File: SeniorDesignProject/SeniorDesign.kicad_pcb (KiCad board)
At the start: 2 copper layers, 31 parts, among them J1 RJ45(LoadCells), J2 RJ45(Accelerometer), J3 PICkit3, J4 RJ11(ICD3), J5 ID-12LA Header, J6 XBEE Header, J7 7-Segment Display, P7 Power 1, P9 Power 2, U1 INA827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

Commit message: added some traces
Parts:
- C1: footprint Capacitors_SMD:C_0201 -> Capacitors_SMD:C_0805
- R1: moved to B.Cu
- moved P7 118.7 mm to (20.0, 59.5)
- moved JP1 116.6 mm to (44.5, 52.0)
- moved U10 114.3 mm to (37.0, 83.5)
- moved C6 112.4 mm to (116.5, 69.1), turned to 90 degrees
- moved C7 108.4 mm to (107.2, 58.5)
- moved R2 102.1 mm to (98.6, 66.1)
- moved JP2 101.3 mm to (42.8, 40.5)
- moved P9 99.2 mm to (21.4, 83.1)
- moved J6 93.4 mm to (82.1, 24.8)
- moved R4 90.5 mm to (121.2, 68.5), turned to 180 degrees
- moved C2 88.3 mm to (101.3, 82.7), turned to 90 degrees
- moved C8 84.8 mm to (113.5, 56.9), turned to 270 degrees
- moved U9 83.6 mm to (51.5, 83.1)
- moved R3 81.7 mm to (121.2, 65.1)
- moved G*** 79.6 mm to (65.6, 128.9)
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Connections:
- CPU1 pad 13: AN0 -> Net-(CPU1-Pad13)
- CPU1 pad 28: Net-(CPU1-Pad28) -> AN0
- CPU1 pad 31: SDA2 -> Net-(CPU1-Pad31)
- CPU1 pad 32: SCL2 -> Net-(CPU1-Pad32)
- CPU1 pad 36: SDA1 -> Net-(CPU1-Pad36)
- CPU1 pad 37: SCL1 -> Net-(CPU1-Pad37)
- CPU1 pad 43: Net-(CPU1-Pad43) -> SDA2
- CPU1 pad 44: Net-(CPU1-Pad44) -> SCL2
- CPU1 pad 45: Net-(CPU1-Pad45) -> UART1RX
- CPU1 pad 46: Net-(CPU1-Pad46) -> UART1TX
- CPU1 pad 48: Net-(CPU1-Pad48) -> SCL1
- CPU1 pad 49: Net-(CPU1-Pad49) -> SDA1
- CPU1 pad 50: UART1TX -> Net-(CPU1-Pad50)
- CPU1 pad 51: UART1RX -> Net-(CPU1-Pad51)
- U1 pad 1: Net-(R1-Pad1) -> A-
- U1 pad 2: A- -> Net-(R1-Pad1)
- U1 pad 3: A+ -> Net-(R1-Pad2)
- U1 pad 4: -5V -> A+
- U1 pad 5: Net-(U1-Pad5) -> -5V
- U1 pad 6: AN0 -> Net-(U1-Pad6)
- U1 pad 7: Net-(U1-Pad7) -> AN0
- U1 pad 8: Net-(R1-Pad2) -> +5V
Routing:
- net GND: track 0.00 -> 91.7 mm
- net UART2RX: track 0.00 -> 59.2 mm, vias 0 -> 2
- net UART2TX: track 0.00 -> 57.5 mm
- net PGEC3: track 0.00 -> 33.3 mm
- net PGED3: track 0.00 -> 32.8 mm, vias 0 -> 2
- net 3.3V: track 0.00 -> 25.8 mm
- net UART1RX: track 0.00 -> 20.5 mm, vias 0 -> 2
- net A+: track 0.00 -> 12.9 mm
- net A-: track 0.00 -> 10.6 mm
- net SCL1: track 0.00 -> 8.48 mm
- net SCL2: track 0.00 -> 7.47 mm
- net +5V: track 0.00 -> 5.66 mm
- net Net-(R1-Pad2): track 0.00 -> 5.29 mm, vias 0 -> 1
- net Net-(R1-Pad1): track 0.00 -> 4.77 mm, vias 0 -> 1
- net Net-(CPU1-Pad7): track 0.00 -> 3.64 mm
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
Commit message: Updates to board
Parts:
- moved G*** 133.3 mm to (197.9, 112.9)
- moved G*** 91.4 mm to (105.5, 41.7)
- moved C6 68.7 mm to (181.9, 90.4), turned to 0 degrees
- moved J5 67.6 mm to (198.2, 81.7)
- moved C2 67.6 mm to (165.8, 103.0)
- moved C7 67.6 mm to (171.7, 78.9)
- moved R5 67.6 mm to (183.9, 78.9)
- moved U9 67.6 mm to (116.0, 103.4)
- moved C1 67.6 mm to (176.7, 102.7)
- moved C8 67.6 mm to (178.0, 77.2)
- moved CPU1 67.6 mm to (172.4, 89.1)
- moved J1 67.6 mm to (167.5, 119.2)
- moved J3 67.6 mm to (136.4, 95.8)
- moved J4 67.6 mm to (87.0, 56.0)
- moved J6 67.6 mm to (146.6, 45.2)
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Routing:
- net GND: track 91.7 -> 35.6 mm
- net 3.3V: track 25.8 -> 21.0 mm
- net Net-(CPU1-Pad7): track 3.64 -> 4.75 mm

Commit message: Updates to board
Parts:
- removed JP1, JP2: Jumper_NO_Small, Pin_Headers:Pin_Header_Straight_1x02_Pitch2.54mm
- added U2: LM1117-3.3, TO_SOT_Packages_SMD:SOT-223, F.Cu at (82.6, 100.6)
- C5, C6, C7: moved to B.Cu
- J5: footprint Pin_Headers:Pin_Header_Straight_2x06_Pitch2.54mm -> Socket_Strips:Socket_Strip_Straight_1x05_Pitch2.54mm
- moved U9 31.0 mm to (97.3, 78.7)
- moved P9 26.6 mm to (81.6, 77.1), turned to 90 degrees
- moved J4 16.2 mm to (87.1, 39.8)
- moved R6 15.4 mm to (180.9, 89.6), turned to 270 degrees
- moved U10 15.0 mm to (110.6, 91.9)
- moved R3 12.1 mm to (182.3, 97.1)
- moved R5 11.8 mm to (183.1, 90.7), turned to 270 degrees
- moved R4 11.4 mm to (182.4, 99.7)
- moved G*** 11.3 mm to (116.5, 44.0)
- moved P7 7.88 mm to (81.6, 87.2), turned to 90 degrees
- moved C7 7.33 mm to (173.4, 86.0)
- moved C5 6.43 mm to (169.4, 89.8), turned to 270 degrees
- moved C6 6.29 mm to (175.6, 90.2), turned to 90 degrees
- moved J5 4.45 mm to (202.5, 82.8)
- moved C4 1.28 mm to (169.6, 97.4), turned to 0 degrees
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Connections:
- net AN0 renamed AN13
- net RFID_LED renamed LED
- C2 pad 2: GND -> Net-(C2-Pad2)
- CPU1 pad 31: Net-(CPU1-Pad31) -> SDA2
- CPU1 pad 32: Net-(CPU1-Pad32) -> SCL2
- CPU1 pad 36: Net-(CPU1-Pad36) -> SDA1
- CPU1 pad 37: Net-(CPU1-Pad37) -> SCL1
- CPU1 pad 43: SDA2 -> Net-(CPU1-Pad43)
- CPU1 pad 44: SCL2 -> Net-(CPU1-Pad44)
- CPU1 pad 45: UART1RX -> Net-(CPU1-Pad45)
- CPU1 pad 46: UART1TX -> Net-(CPU1-Pad46)
- CPU1 pad 48: SCL1 -> Net-(CPU1-Pad48)
- CPU1 pad 49: SDA1 -> Net-(CPU1-Pad49)
- CPU1 pad 50: Net-(CPU1-Pad50) -> UART1TX
- CPU1 pad 51: Net-(CPU1-Pad51) -> UART1RX
- J5 pad 2: Net-(J5-Pad2) -> GND
- J5 pad 4: GND -> UART1RX
- J5 pad 5: UART1RX -> CP
- P7 pad 1: Net-(P7-Pad1) -> GND
- P9 pad 2: Net-(P9-Pad2) -> GND
- R5 pad 2: SCL1 -> SDA1
- R6 pad 2: SDA1 -> SCL1
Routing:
- net UART1RX: track 20.4 -> 0.00 mm, vias 2 -> 0
- net GND: track 35.6 -> 45.8 mm, vias 0 -> 5
- net SDA2: track 0.00 -> 8.41 mm
- net SDA1: track 0.00 -> 5.89 mm
- net SCL1: track 8.48 -> 2.89 mm
- net 3.3V: track 21.0 -> 24.2 mm, vias 0 -> 7
- net (no net): track 0.15 -> 1.49 mm
- net Net-(C2-Pad2): track 0.00 -> 1.23 mm
- net SCL2: track 7.47 -> 6.53 mm
- added copper zone on B.Cu, net 3.3V
- added copper zone on F.Cu, net GND

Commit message: Updates
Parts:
- removed J4: RJ11(ICD3), SeniorDesignFootprints:RJ11-6
- U10, U9: footprint TO_SOT_Packages_THT:TO-220_Horizontal -> TO_SOT_Packages_THT:TO-92_Inline_Wide
- moved G*** 70.9 mm to (129.0, 113.8)
- moved U2 39.4 mm to (120.7, 90.3), turned to 270 degrees
- moved J7 28.5 mm to (183.3, 67.1)
- moved P9 26.6 mm to (92.2, 101.5)
- moved J6 24.7 mm to (126.5, 59.4)
- moved J2 22.9 mm to (165.7, 65.2)
- moved U9 12.8 mm to (104.5, 89.3), turned to 90 degrees
- moved U10 12.4 mm to (104.8, 102.9), turned to 90 degrees
- moved P7 10.3 mm to (91.4, 90.0)
- moved G*** 7.58 mm to (195.1, 119.9)
- moved R1 1.24 mm to (171.7, 110.0)
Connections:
- CPU1 pad 46: Net-(CPU1-Pad46) -> UART1RX
- CPU1 pad 51: UART1RX -> Net-(CPU1-Pad51)
- P7 pad 2: Net-(P7-Pad2) -> +9V
- P9 pad 1: Net-(P9-Pad1) -> -9V
- U10 pad 1: (no net) -> -5V
- U10 pad 2: (no net) -> -9V
- U10 pad 3: (no net) -> GND
- U9 pad 1: (no net) -> +5V
- U9 pad 2: (no net) -> GND
- U9 pad 3: (no net) -> +9V
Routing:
- net +5V: track 5.66 -> 85.0 mm, vias 0 -> 3
- net UART2RX: track 59.2 -> 0.00 mm, vias 2 -> 0
- net UART2TX: track 57.5 -> 1.26 mm
- net UART1RX: track 0.00 -> 26.0 mm
- net GND: track 45.8 -> 30.1 mm
- net Net-(R1-Pad2): track 5.29 -> 3.86 mm
- net Net-(R1-Pad1): track 4.77 -> 3.75 mm

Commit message: Updated board layout and design
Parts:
- added ?: 1pin, Connectors:1pin, F.Cu at (182.6, 117.3)
- added ?: 1pin, Connectors:1pin, F.Cu at (120.4, 116.8)
- added REF**: 1pin, Connectors:1pin, F.Cu at (120.1, 60.2)
- added REF**: 1pin, Connectors:1pin, F.Cu at (182.6, 60.2)
- R1: moved to F.Cu
- moved G*** 59.4 mm to (168.1, 69.1)
- moved C1 52.9 mm to (125.0, 91.7), turned to 270 degrees
- moved R1 51.5 mm to (120.9, 101.3)
- moved U1 51.2 mm to (120.9, 96.5)
- moved C2 46.9 mm to (120.4, 91.2)
- moved G*** 46.8 mm to (167.1, 82.3)
- moved J6 46.2 mm to (138.9, 103.9), turned to 90 degrees
- moved J7 44.3 mm to (138.9, 67.8)
- moved U10 42.3 mm to (131.8, 70.4)
- moved P9 38.5 mm to (121.9, 77.0)
- moved C4 36.6 mm to (135.6, 83.6), turned to 270 degrees
- moved R4 35.9 mm to (148.6, 87.6), turned to 0 degrees
- moved J2 33.0 mm to (172.2, 97.5), turned to 0 degrees
- moved R3 32.8 mm to (151.6, 85.6), turned to 90 degrees
- moved R5 32.6 mm to (151.6, 82.3), turned to 90 degrees
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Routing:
- net +5V: track 85.0 -> 0.00 mm, vias 3 -> 0
- net PGEC3: track 33.3 -> 0.00 mm
- net PGED3: track 32.8 -> 0.00 mm, vias 2 -> 0
- net GND: track 30.1 -> 0.00 mm, vias 5 -> 0
- net UART1RX: track 26.0 -> 0.00 mm
- net 3.3V: track 24.2 -> 0.51 mm, vias 7 -> 0
- net A+: track 12.9 -> 0.00 mm
- net A-: track 10.6 -> 0.00 mm
- net SDA2: track 8.41 -> 0.00 mm
- net SCL2: track 6.53 -> 0.00 mm
- net SDA1: track 5.89 -> 0.00 mm
- net Net-(CPU1-Pad7): track 4.75 -> 0.00 mm
- net -5V: track 3.90 -> 0.00 mm
- net Net-(R1-Pad2): track 3.86 -> 0.00 mm, vias 1 -> 0
- net Net-(R1-Pad1): track 3.75 -> 0.00 mm, vias 1 -> 0
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- removed copper zone on B.Cu, net 3.3V
- removed copper zone on F.Cu, net GND
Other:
- board text added: "Hardware: Tanner Daniels & Jack L. Wolfe III Software: Mark Archual & Ethan Schweinsberg"
- board text removed: "Hardware: Tanner Daniels and Jack L. Wolfe III Software: Mark Archual and Ethan Schweinsberg"

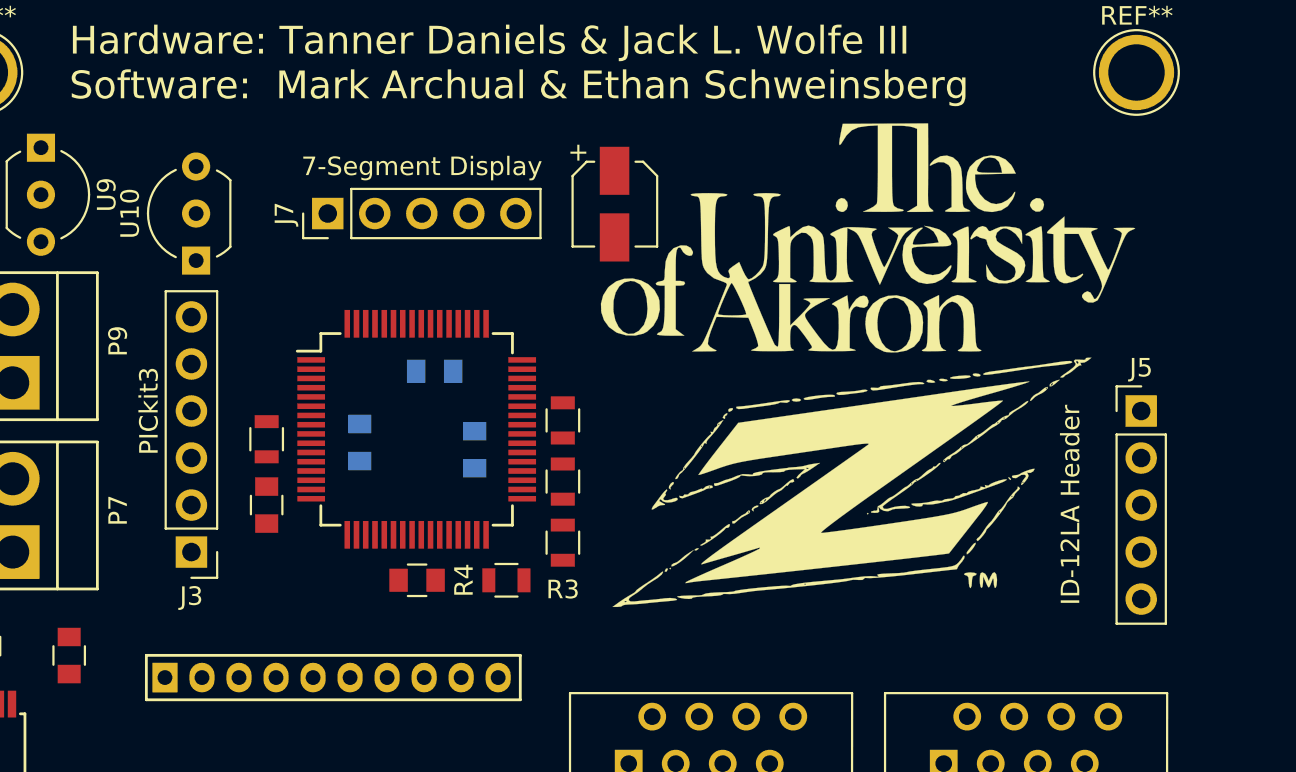
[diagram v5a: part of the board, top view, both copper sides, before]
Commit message: Added TL7660 +5V ro -5V converter, Removed 7905 Regulator Removed -9V connection
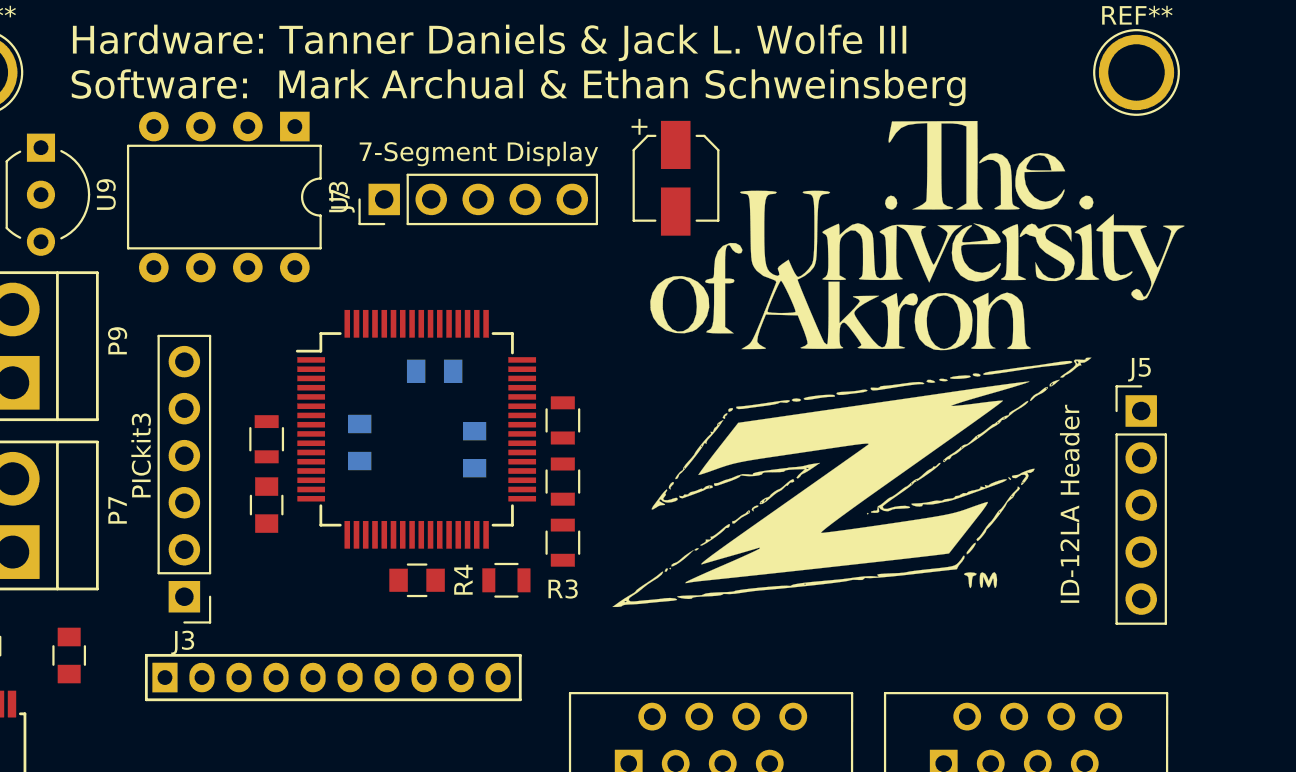
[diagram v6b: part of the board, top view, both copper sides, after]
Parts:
- removed U10: 7905, TO_SOT_Packages_THT:TO-92_Inline_Wide
- added U3: ICL7660, Housings_DIP:DIP-8_W7.62mm, F.Cu at (137.2, 63.1)
- moved C8 3.59 mm to (157.7, 65.9)
- moved J7 3.14 mm to (142.0, 67.1)
- moved G*** 2.67 mm to (170.8, 69.0)
- moved J3 2.44 mm to (131.2, 88.5)
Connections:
- U9 pad 1: +5V -> (no net)
- U9 pad 2: GND -> (no net)
- U9 pad 3: +9V -> (no net)
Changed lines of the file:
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@@
 (kicad_pcb (version 4) (host pcbnew 4.0.6-e0-6349~53~ubuntu16.04.1)
   (general
-    (links 69)
-    (no_connects 69)
+    (links 66)
+    (no_connects 66)
     (area 116.739999 56.175 186.028001 121.766001)
     (thickness 1.6)
@@
     (zones 0)
     (modules 33)
-    (nets 98)
+    (nets 103)
   )
   (page USLetter)
@@
   (net 96 +9V)
   (net 97 -9V)
+  (net 98 "Net-(U3-Pad1)")
+  (net 99 "Net-(U3-Pad2)")
+  (net 100 "Net-(U3-Pad6)")
+  (net 101 "Net-(U3-Pad7)")
+  (net 102 "Net-(U3-Pad4)")
   (net_class Default "This is the default net class."
     (clearance 0.2)
@@
     (add_net "Net-(R1-Pad2)")
     (add_net "Net-(U1-Pad6)")
+    (add_net "Net-(U3-Pad1)")
+    (add_net "Net-(U3-Pad2)")
+    (add_net "Net-(U3-Pad4)")
+    (add_net "Net-(U3-Pad6)")
+    (add_net "Net-(U3-Pad7)")
     (add_net PGEC3)
     (add_net PGED3)
@@
   )
   (module SeniorDesignFootprints:Uakron (layer F.Cu)
-    (at 168.148 69.088)
+    (at 170.815 68.961)
     (fp_text reference G*** (at 0.23 -10.41) (layer F.SilkS) hide
       (effects (font (thickness 0.3)))
@@
   )
   (module Capacitors_SMD:CP_Elec_4x4.5 (layer F.Cu)
-    (at 154.432 67.31 270)
+    (at 157.734 65.913 270)
     (descr "SMT capacitor, aluminium electrolytic, 4x4.5")
     (attr smd)
@@
   )
   (module Pin_Headers:Pin_Header_Straight_1x06_Pitch2.54mm (layer F.Cu)
-    (at 131.572 86.106 180)
+    (at 131.191 88.519 180)
     (descr "Through hole straight pin header, 1x06, 2.54mm pitch, single row")
     (tags "Through hole pin header THT 1x06 2.54mm single row")
@@
   )
   (module Socket_Strips:Socket_Strip_Straight_1x05_Pitch2.54mm (layer F.Cu)
-    (at 138.938 67.818 90)
+    (at 141.986 67.056 90)
     (descr "Through hole straight socket strip, 1x05, 2.54mm pitch, single row")
     (tags "Through hole socket strip THT 1x05 2.54mm single row")
@@
     (fp_arc (start 2.54 0) (end 2.54 -2.48) (angle -135) (layer F.Fab) (width 0.1))
     (fp_arc (start 2.54 0) (end 4.34 1.85) (angle -20) (layer F.SilkS) (width 0.12))
-    (pad 2 thru_hole circle (at 2.54 0) (size 1.52 1.52) (drill 0.8) (layers *.Cu *.Mask)
-      (net 45 GND))
-    (pad 3 thru_hole circle (at 5.08 0) (size 1.52 1.52) (drill 0.8) (layers *.Cu *.Mask)
-      (net 96 +9V))
-    (pad 1 thru_hole rect (at 0 0 270) (size 1.52 1.52) (drill 0.8) (layers *.Cu *.Mask)
-      (net 51 +5V))
-    (model TO_SOT_Packages_THT.3dshapes/TO-92_Inline_Wide.wrl
-      (at (xyz 0.1 0 0))
-      (scale (xyz 1 1 1))
-      (rotate (xyz 0 0 -90))
-    )
-  )
-  (module TO_SOT_Packages_THT:TO-92_Inline_Wide (layer F.Cu)
-    (at 131.826 70.358 90)
-    (descr "TO-92 leads in-line, wide, drill 0.8mm (see NXP sot054_po.pdf)")
-    (tags "to-92 sc-43 sc-43a sot54 PA33 transistor")
-    (fp_text reference U10 (at 2.54 -3.56 270) (layer F.SilkS)
-      (effects (font (size 1 1) (thickness 0.15)))
-    )
-    (fp_text value 7905 (at 2.54 2.79 90) (layer F.Fab)
-      (effects (font (size 1 1) (thickness 0.15)))
-    )
-    (fp_text user %R (at 2.54 -3.56 270) (layer F.Fab)
-      (effects (font (size 1 1) (thickness 0.15)))
-    )
-    (fp_line (start 0.74 1.85) (end 4.34 1.85) (layer F.SilkS) (width 0.12))
-    (fp_line (start 0.8 1.75) (end 4.3 1.75) (layer F.Fab) (width 0.1))
-    (fp_line (start -1.01 -2.73) (end 6.09 -2.73) (layer F.CrtYd) (width 0.05))
-    (fp_line (start -1.01 -2.73) (end -1.01 2.01) (layer F.CrtYd) (width 0.05))
-    (fp_line (start 6.09 2.01) (end 6.09 -2.73) (layer F.CrtYd) (width 0.05))
-    (fp_line (start 6.09 2.01) (end -1.01 2.01) (layer F.CrtYd) (width 0.05))
-    (fp_arc (start 2.54 0) (end 0.74 1.85) (angle 20) (layer F.SilkS) (width 0.12))
-    (fp_arc (start 2.54 0) (end 2.54 -2.6) (angle -65) (layer F.SilkS) (width 0.12))
-    (fp_arc (start 2.54 0) (end 2.54 -2.6) (angle 65) (layer F.SilkS) (width 0.12))
-    (fp_arc (start 2.54 0) (end 2.54 -2.48) (angle 135) (layer F.Fab) (width 0.1))
-    (fp_arc (start 2.54 0) (end 2.54 -2.48) (angle -135) (layer F.Fab) (width 0.1))
-    (fp_arc (start 2.54 0) (end 4.34 1.85) (angle -20) (layer F.SilkS) (width 0.12))
-    (pad 2 thru_hole circle (at 2.54 0 180) (size 1.52 1.52) (drill 0.8) (layers *.Cu *.Mask)
-      (net 97 -9V))
-    (pad 3 thru_hole circle (at 5.08 0 180) (size 1.52 1.52) (drill 0.8) (layers *.Cu *.Mask)
-      (net 45 GND))
-    (pad 1 thru_hole rect (at 0 0 90) (size 1.52 1.52) (drill 0.8) (layers *.Cu *.Mask)
-      (net 46 -5V))
+    (pad 2 thru_hole circle (at 2.54 0) (size 1.52 1.52) (drill 0.8) (layers *.Cu *.Mask))
+    (pad 3 thru_hole circle (at 5.08 0) (size 1.52 1.52) (drill 0.8) (layers *.Cu *.Mask))
+    (pad 1 thru_hole rect (at 0 0 270) (size 1.52 1.52) (drill 0.8) (layers *.Cu *.Mask))
     (model TO_SOT_Packages_THT.3dshapes/TO-92_Inline_Wide.wrl
       (at (xyz 0.1 0 0))
@@
     (pad 1 thru_hole circle (at 0 0) (size 4.064 4.064) (drill 3.048) (layers *.Cu *.Mask))
   )
+  (module Housings_DIP:DIP-8_W7.62mm (layer F.Cu)
+    (at 137.16 63.119 270)
+    (descr "8-lead dip package, row spacing 7.62 mm (300 mils)")
+    (tags "DIL DIP PDIP 2.54mm 7.62mm 300mil")
+    (fp_text reference U3 (at 3.81 -2.39 270) (layer F.SilkS)
+      (effects (font (size 1 1) (thickness 0.15)))
+    )
+    (fp_text value ICL7660 (at 3.81 10.01 270) (layer F.Fab)
+      (effects (font (size 1 1) (thickness 0.15)))
+    )
+    (fp_arc (start 3.81 -1.39) (end 2.81 -1.39) (angle -180) (layer F.SilkS) (width 0.12))
+    (fp_line (start 1.635 -1.27) (end 6.985 -1.27) (layer F.Fab) (width 0.1))
+    (fp_line (start 6.985 -1.27) (end 6.985 8.89) (layer F.Fab) (width 0.1))
+    (fp_line (start 6.985 8.89) (end 0.635 8.89) (layer F.Fab) (width 0.1))
+    (fp_line (start 0.635 8.89) (end 0.635 -0.27) (layer F.Fab) (width 0.1))
+    (fp_line (start 0.635 -0.27) (end 1.635 -1.27) (layer F.Fab) (width 0.1))
+    (fp_line (start 2.81 -1.39) (end 1.04 -1.39) (layer F.SilkS) (width 0.12))
+    (fp_line (start 1.04 -1.39) (end 1.04 9.01) (layer F.SilkS) (width 0.12))
+    (fp_line (start 1.04 9.01) (end 6.58 9.01) (layer F.SilkS) (width 0.12))
+    (fp_line (start 6.58 9.01) (end 6.58 -1.39) (layer F.SilkS) (width 0.12))
+    (fp_line (start 6.58 -1.39) (end 4.81 -1.39) (layer F.SilkS) (width 0.12))
+    (fp_line (start -1.1 -1.6) (end -1.1 9.2) (layer F.CrtYd) (width 0.05))
+    (fp_line (start -1.1 9.2) (end 8.7 9.2) (layer F.CrtYd) (width 0.05))
+    (fp_line (start 8.7 9.2) (end 8.7 -1.6) (layer F.CrtYd) (width 0.05))
+    (fp_line (start 8.7 -1.6) (end -1.1 -1.6) (layer F.CrtYd) (width 0.05))
+    (pad 1 thru_hole rect (at 0 0 270) (size 1.6 1.6) (drill 0.8) (layers *.Cu *.Mask)
+      (net 98 "Net-(U3-Pad1)"))
+    (pad 5 thru_hole oval (at 7.62 7.62 270) (size 1.6 1.6) (drill 0.8) (layers *.Cu *.Mask)
+      (net 46 -5V))
+    (pad 2 thru_hole oval (at 0 2.54 270) (size 1.6 1.6) (drill 0.8) (layers *.Cu *.Mask)
+      (net 99 "Net-(U3-Pad2)"))
+    (pad 6 thru_hole oval (at 7.62 5.08 270) (size 1.6 1.6) (drill 0.8) (layers *.Cu *.Mask)
+      (net 100 "Net-(U3-Pad6)"))
+    (pad 3 thru_hole oval (at 0 5.08 270) (size 1.6 1.6) (drill 0.8) (layers *.Cu *.Mask)
+      (net 45 GND))
+    (pad 7 thru_hole oval (at 7.62 2.54 270) (size 1.6 1.6) (drill 0.8) (layers *.Cu *.Mask)
+      (net 101 "Net-(U3-Pad7)"))
+    (pad 4 thru_hole oval (at 0 7.62 270) (size 1.6 1.6) (drill 0.8) (layers *.Cu *.Mask)
+      (net 102 "Net-(U3-Pad4)"))
+    (pad 8 thru_hole oval (at 7.62 0 270) (size 1.6 1.6) (drill 0.8) (layers *.Cu *.Mask)
+      (net 51 +5V))
+    (model Housings_DIP.3dshapes/DIP-8_W7.62mm.wrl
+      (at (xyz 0 0 0))
+      (scale (xyz 1 1 1))
+      (rotate (xyz 0 0 0))
+    )
+  )
   (gr_line (start 116.84 121.666) (end 116.84 56.388) (angle 90) (layer Dwgs.User) (width 0.2))
